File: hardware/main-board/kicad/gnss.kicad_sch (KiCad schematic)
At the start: 39 parts, among them J301 U.FL, J302 UM980_AUX, U301 UM980, U302 TPS22945DCKR

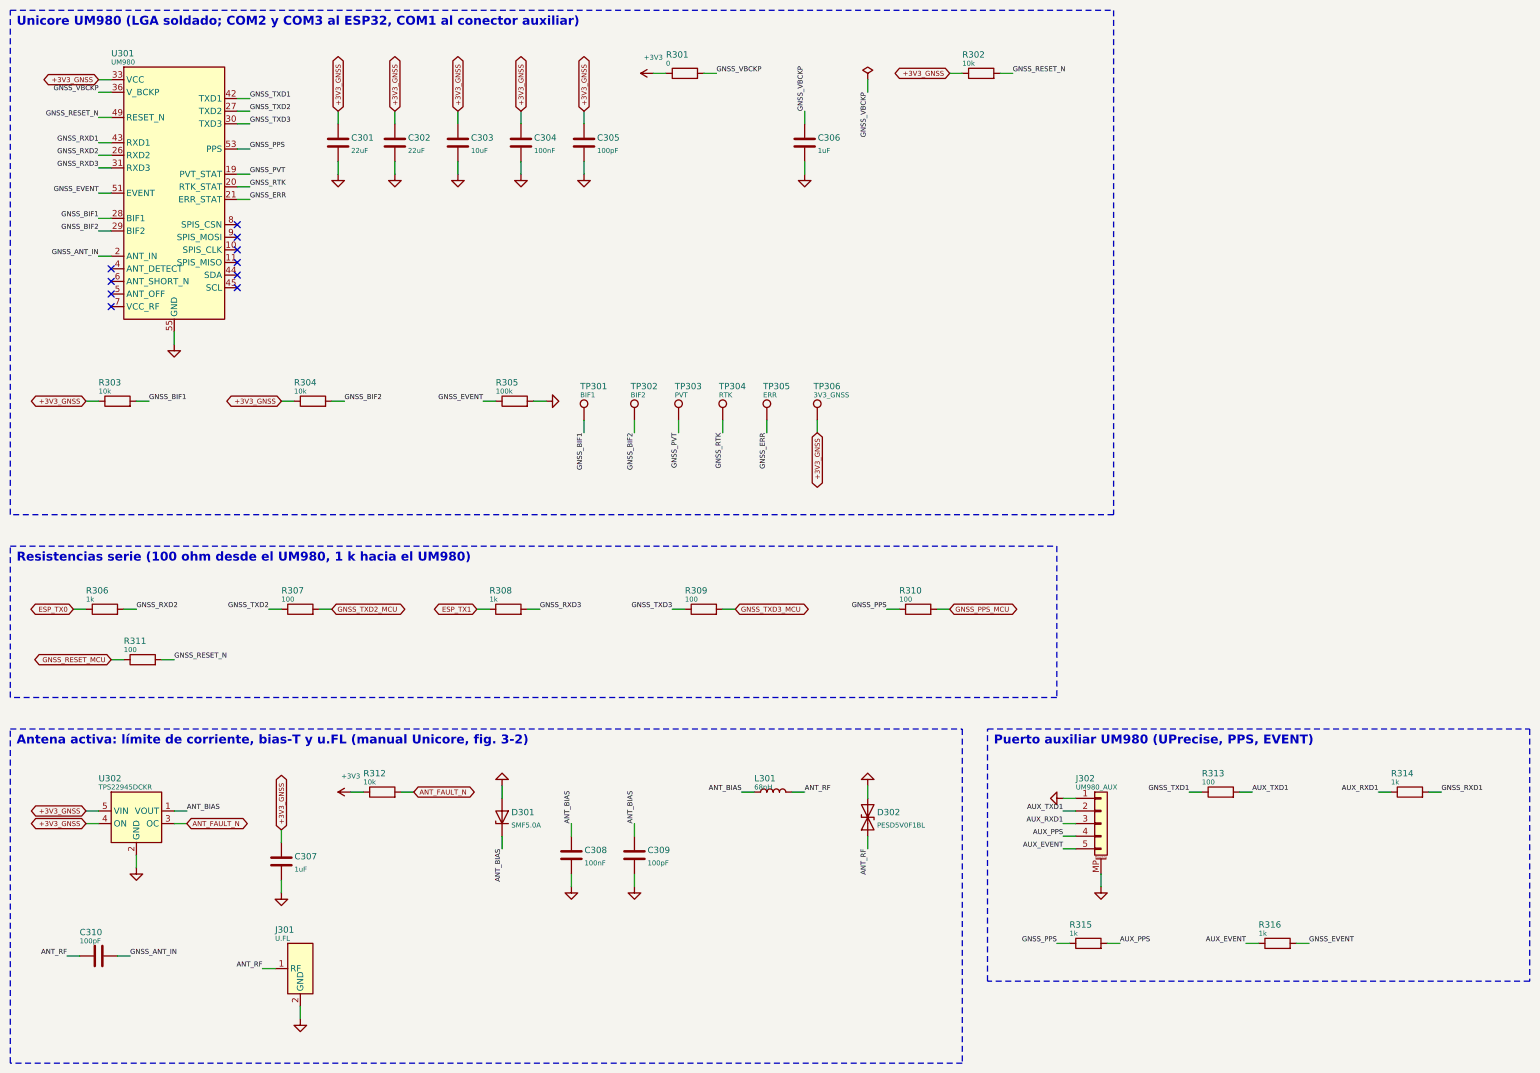
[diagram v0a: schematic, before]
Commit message: Placa principal v0.2: UM980 y BMI088 por cable, conectores hacia cantos o zonas libres, placa panel-usb y un solo panel para JLCPCB
- 46 x 64 mm, 4 capas. El UM980 queda en su carrier BDLX por J301 (GH 8) con 5 V conmutable
  (TPS63070, GPIO45) y el BMI088 vuelve a la tapa por I2C en un segundo bus (J405, GH 7).
- Todos los conectores de cable son GH o SH de 8 pines o menos (kit del propietario), salvo la
  batería (PH 2). Cada uno apunta a un canto o a una zona libre con sitio para la clavija
  enchufada y su cable: áreas de regla clavija_* en el DRC y kicad/plugs.json para el CAD.
- La placa sube 2.5 mm en el tubo (z 23.5-87.5) para que las clavijas del canto inferior tengan
  7.6 mm hasta la base; rieles propuestos en z 39-90 y agujeros nuevos. Comprobada en FreeCAD
  contra V2.2 con modelos 3D y clavijas: sin choques.
- Cargador según el ejemplo de TI: bootstrap junto a sus pines (0.9 y 1.6 mm), salida en abanico
  de la fila inferior y potencia solo por capas externas.
- Placa panel-usb (USB-C a ras de la tapa del panel, GH 8 a J101) y panel de las dos placas con un
  BOM y un CPL (panelize.py, 82.8 x 78 mm).
- Serigrafía sin solapes (silk_clean.py) y logotipo de TresVizo con www.tresvizo.com.
- ERC 0; DRC con 0 errores, 0 avisos, 0 sin conectar y 0 diferencias de paridad en las dos
  placas y el panel. Costo estimado de montaje y piezas: 211 USD por 5 juegos en un panel, sin
  el PCB desnudo.
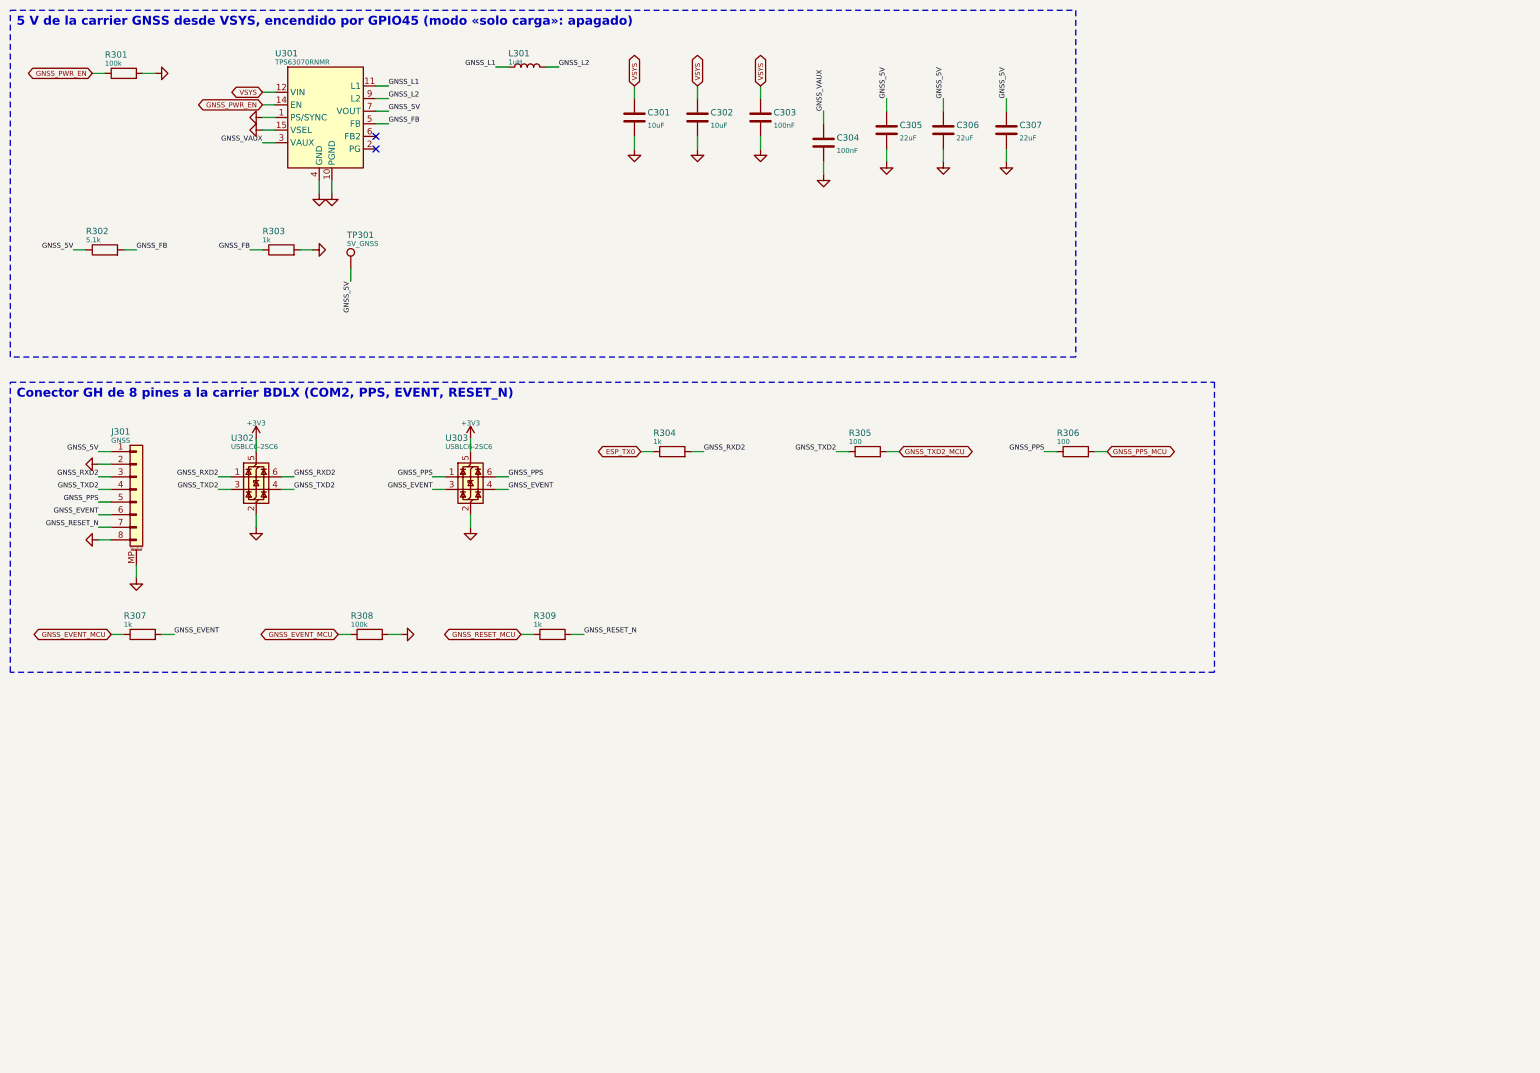
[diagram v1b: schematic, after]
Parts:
- removed C308: 100nF, Capacitor_SMD:C_0402_1005Metric, symbol Device:C
- removed C309, C310: 100pF, Capacitor_SMD:C_0402_1005Metric, symbol Device:C
- removed D301: SMF5.0A, tresvizo_lcsc:SOD-123FL_L2.7-W1.8-LS3.8-RD, symbol Device:D_Zener
- removed D302: PESD5V0F1BL, tresvizo_lcsc:SOD-882_L1.0-W0.6-BI, symbol Device:D_TVS
- removed J302: UM980_AUX, tresvizo_lcsc:CONN-SMD_5P-P1.00_BM05B-SRSS-TB, symbol Connector_Generic_MountingPin:Conn_01x05_MountingPin
- removed R310, R311, R313: 100, Resistor_SMD:R_0402_1005Metric, symbol Device:R
- removed R312: 10k, Resistor_SMD:R_0402_1005Metric, symbol Device:R
- removed R314, R315, R316: 1k, Resistor_SMD:R_0402_1005Metric, symbol Device:R
- removed TP302: BIF2, TestPoint:TestPoint_Pad_D1.0mm, symbol Connector:TestPoint
- removed TP303: PVT, TestPoint:TestPoint_Pad_D1.0mm, symbol Connector:TestPoint
- removed TP304: RTK, TestPoint:TestPoint_Pad_D1.0mm, symbol Connector:TestPoint
- removed TP305: ERR, TestPoint:TestPoint_Pad_D1.0mm, symbol Connector:TestPoint
- removed TP306: 3V3_GNSS, TestPoint:TestPoint_Pad_D1.0mm, symbol Connector:TestPoint
- added U303: USBLC6-2SC6, tresvizo_lcsc:SOT-23-6_L2.9-W1.6-P0.95-LS2.8-BL, symbol Power_Protection:USBLC6-2SC6
- C301, C302: value 22uF -> 10uF; LCSC C45783 -> C15850; MPN CL21A226MAQNNNE -> CL21A106KAYNNNE
- C303: value 10uF -> 100nF; footprint Capacitor_SMD:C_0805_2012Metric -> Capacitor_SMD:C_0402_1005Metric; LCSC C15850 -> C307331; MPN CL21A106KAYNNNE -> CL05B104KB54PNC
- C305: value 100pF -> 22uF; footprint Capacitor_SMD:C_0402_1005Metric -> Capacitor_SMD:C_0805_2012Metric; LCSC C1546 -> C45783; MPN 0402CG101J500NT -> CL21A226MAQNNNE
- C306, C307: value 1uF -> 22uF; footprint Capacitor_SMD:C_0402_1005Metric -> Capacitor_SMD:C_0805_2012Metric; LCSC C52923 -> C45783; MPN CL05A105KA5NQNC -> CL21A226MAQNNNE
- J301: value U.FL -> GNSS; footprint tresvizo_lcsc:IPEX-SMD_BWIPX-1-001E -> tresvizo_lcsc:CONN-SMD_8P-P1.25_XUNPU-WAFER-GH1.25-8PWB; symbol tresvizo:U.FL -> Connector_Generic_MountingPin:Conn_01x08_MountingPin; LCSC C5137195 -> C3029383; MPN BWU.FL-IPEX1 -> WAFER-GH1.25-8PWB
- L301: value 68nH -> 1uH; footprint tresvizo_lcsc:L0603 -> tresvizo_lcsc:L2520; LCSC C86135 -> C435392; MPN LQW18AN68NG00D -> DFE252012F-1R0M=P2
- R301: value 0 -> 100k; LCSC C17168 -> C25741; MPN 0402WGF0000TCE -> 0402WGF1003TCE
- R302: value 10k -> 5.1k; LCSC C25744 -> C25905; MPN 0402WGF1002TCE -> 0402WGF5101TCE
- R303, R304: value 10k -> 1k; LCSC C25744 -> C11702; MPN 0402WGF1002TCE -> 0402WGF1001TCE
- R305: value 100k -> 100; LCSC C25741 -> C25076; MPN 0402WGF1003TCE -> 0402WGF1000TCE
- R306: value 1k -> 100; LCSC C11702 -> C25076; MPN 0402WGF1001TCE -> 0402WGF1000TCE
- R307, R309: value 100 -> 1k; LCSC C25076 -> C11702; MPN 0402WGF1000TCE -> 0402WGF1001TCE
- R308: value 1k -> 100k; LCSC C11702 -> C25741; MPN 0402WGF1001TCE -> 0402WGF1003TCE
- TP301: value BIF1 -> 5V_GNSS
- U301: value UM980 -> TPS63070RNMR; footprint tresvizo:UM980 -> tresvizo_lcsc:VQFN-15_L3.0-W2.5-P0.50-BL; symbol tresvizo:UM980 -> tresvizo:TPS63070; LCSC (none) -> C109322; MPN UM980 -> TPS63070RNMR
- U302: value TPS22945DCKR -> USBLC6-2SC6; footprint tresvizo_lcsc:SC-70-5_L2.1-W1.3-P0.65-LS2.1-BL -> tresvizo_lcsc:SOT-23-6_L2.9-W1.6-P0.95-LS2.8-BL; symbol tresvizo:TPS22945 -> Power_Protection:USBLC6-2SC6; LCSC C47507 -> C2687116; MPN TPS22945DCKR -> USBLC6-2SC6
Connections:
- net ANT_FAULT_N is gone; now on net GNSS_TXD2: U302.3 (I/O2)
- net GNSS_TXD3_MCU is gone; now on net GNSS_RESET_N: R309.2
- net +3V3: now also U302.5 (VBUS), U303.5 (VBUS); no longer R301.1
- net ESP_TX0: now also R304.1; no longer R306.1
- net GND: now also J301.8 (Pin_8), J301.MP (MountPin), R301.2, R303.2, R308.2, U301.10 (PGND), U301.15 (VSEL), U301.4 (GND), U303.2 (GND); no longer J301.3 (GND), R305.2, U301.12 (GND), U301.14 (GND), U301.3 (GND), U301.32 (GND), U301.37 (GND), U301.41 (GND), U301.48 (GND), U301.55 (GND)
- net GNSS_EVENT: now also J301.6 (Pin_6), R307.2, U303.3 (I/O2), U303.4 (I/O2); no longer R305.1, U301.51 (EVENT)
- net GNSS_PPS: now also J301.5 (Pin_5), R306.1, U303.1 (I/O1), U303.6 (I/O1); no longer U301.53 (PPS)
- net GNSS_PPS_MCU: now also R306.2
- net GNSS_RESET_MCU: now also R309.1
- net GNSS_RESET_N: now also J301.7 (Pin_7); no longer R302.2, U301.49 (RESET_N)
- net GNSS_RXD2: now also J301.3 (Pin_3), R304.2, U302.1 (I/O1), U302.6 (I/O1); no longer R306.2, U301.26 (RXD2)
- net GNSS_TXD2: now also J301.4 (Pin_4), R305.1, U302.4 (I/O2); no longer R307.1, U301.27 (TXD2)
- net GNSS_TXD2_MCU: now also R305.2; no longer R307.2
- net GNSS_L1: now reaches U301.11 (L1)
- net GNSS_L1: now also L301.1
- net GNSS_FB: now reaches U301.5 (FB)
- net GNSS_FB: now also R302.2, R303.1
- net GNSS_5V: now reaches U301.7 (VOUT)
- net GNSS_5V: now also C305.1, C306.1, C307.1, J301.1 (Pin_1), R302.1, TP301.1
- net GNSS_L2: now reaches U301.9 (L2)
- net GNSS_L2: now also L301.2
- removed net +3V3_GNSS: C301.1, C302.1, C303.1, C304.1, C305.1, C307.1, R302.1, R303.1, R304.1, U301.33 (VCC), U301.34 (VCC), U302.4 (ON), U302.5 (VIN)
- removed net ANT_BIAS: L301.1, U302.1 (VOUT)
- removed net ANT_RF: J301.1 (RF), L301.2
- net ESP_TX1 renamed GNSS_EVENT_MCU
- net GNSS_EVENT_MCU: now also R307.1
- net GNSS_ANT_IN: no longer names the net of U301.2 (PG)
- removed net GNSS_BIF1: R303.2, TP301.1, U301.28 (BIF1)
- removed net GNSS_BIF2: R304.2, U301.29 (BIF2)
- removed net GNSS_ERR: U301.21 (ERR_STAT)
- removed net GNSS_PVT: U301.19 (PVT_STAT)
- removed net GNSS_RTK: U301.20 (RTK_STAT)
- removed net GNSS_RXD1: U301.43 (RXD1)
- removed net GNSS_RXD3: R308.2, U301.31 (RXD3)
- removed net GNSS_TXD1: U301.42 (TXD1)
- removed net GNSS_TXD3: R309.1, U301.30 (TXD3)
- removed net GNSS_VBCKP: C306.1, R301.2, U301.36 (V_BCKP)
- new net GNSS_PWR_EN: R301.1, U301.14 (EN)
- new net GNSS_VAUX: C304.1, U301.3 (VAUX)
- new net VSYS: C301.1, C302.1, C303.1, U301.12 (VIN)
- no-connect marks 10 -> 2
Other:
- note added: "5 V de la carrier GNSS desde VSYS, encendido por GPIO45 (modo «solo carga»: apagado)"
- note added: "Conector GH de 8 pines a la carrier BDLX (COM2, PPS, EVENT, RESET_N)"
- note removed: "Antena activa: límite de corriente, bias-T y u.FL (manual Unicore, fig. 3-2)"
- note removed: "Puerto auxiliar UM980 (UPrecise, PPS, EVENT)"
- note removed: "Resistencias serie (100 ohm desde el UM980, 1 k hacia el UM980)"
- note removed: "Unicore UM980 (LGA soldado; COM2 y COM3 al ESP32, COM1 al conector auxiliar)"
- title: GNSS UM980 y antena -> GNSS: carrier UM980 por conector y su 5 V
- moved on the sheet: C301, C302, C303, C304, C305, C306, C307, L301, R301, R302, R303, R304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

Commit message: Placa principal v0.2: ESP32-S3-WROOM-1-N16R2 en lugar del MINI-1 y sin LEDs del panel
- U201 = ESP32-S3-WROOM-1-N16R2 (C2913205): 16 MB de flash y 2 MB de PSRAM quad. Huella y
  modelos de LCSC; el .step se corrió 3.65 mm para que coincida con su .wrl y la huella.
- GPIO nuevos para rutear el módulo en la misma placa: microSD CLK 6, CMD 7, D0 5, D1 4, D2 16,
  D3 15 y detección 17; UART del GNSS TX 8 / RX 9; PPS 10, EVENT 11, RESET 12; I2C 13/14;
  IMU 41/42 con INT1 2 e INT3 1; botón 18; puntos de prueba en 35, 36 y 37. README y pinout
  con el mapa para el firmware.
- Fuera J406, sus resistencias y la del STAT del cargador: la carcasa V2.3 no lleva LEDs.
- Misma placa de 46 x 64 mm. H1 pasa a (12.0, 9.6) y el corte del riel +X frente a la antena a
  v 15.1-34.0; antena sin cobre en u 0-6.7, v 15.7-33.7.
- R108 sale de debajo de los pines de la microSD (el ruteador se ciclaba entre SD_D3 y
  CHG_INT_N) y el divisor de TS va bajo L102.
- BUCK_SW y el PGND de U105 prerruteados: la vía que el ruteador ponía junto a L102 hacía caer
  el relleno de zonas de KiCad 10 (-11, también en kicad-cli). route_rest guarda las pistas que
  arranca mientras dura el ruteo.
- DRC 0, sin conexiones pendientes y con paridad en la placa y en el panel; ERC 0. Costo
  estimado 206.86 USD por 5 juegos (montaje + piezas, sin PCB).
- Carcasa V2.3: H1 en z 77.9, riel +X cortado en z 53.7-72.4, placa superior recortada frente
  a la antena y SMA de la carrier con las medidas de la foto. Placa nueva contra la carcasa:
  0 mm3 de choques.
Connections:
- net ESP_TX0 renamed GNSS_TX_MCU
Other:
- moved on the sheet: R304, R305, R306
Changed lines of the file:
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@@
 		(company "TresVizo")
 		(comment 1 "Exploratorio: no fabricado ni probado")
-		(comment 2 "ESP32-S3-MINI-1-N4R2 + BQ25798 (1S; 2S por variante); GNSS e IMU por conector")
+		(comment 2 "ESP32-S3-WROOM-1-N16R2 + BQ25798 (1S; 2S por variante); GNSS e IMU por conector")
 		(comment 3 "JLCPCB 4 capas JLC04161H-7628")
 	)
@@
 	(symbol
 		(lib_id "Device:R")
-		(at 146.05 106.68 90)
+		(at 149.86 106.68 90)
 		(unit 1)
 		(exclude_from_sim no)
@@
 		(dnp no)
 		(property "Reference" "R304"
-			(at 142.24 103.664 270)
+			(at 146.05 103.664 270)
 			(effects
 				(font
@@
 		)
 		(property "Value" "1k"
-			(at 142.24 105.264 270)
+			(at 146.05 105.264 270)
 			(effects
 				(font
@@
 		)
 		(property "Footprint" "Resistor_SMD:R_0402_1005Metric"
-			(at 146.05 106.68 0)
+			(at 149.86 106.68 0)
 			(effects
 				(font
@@
 		)
 		(property "Datasheet" ""
-			(at 146.05 106.68 0)
+			(at 149.86 106.68 0)
 			(effects
 				(font
@@
 			)
 		)
-		(property "Description" "GPIO43 (U0TXD) -> RXD2 de la carrier"
-			(at 146.05 106.68 0)
+		(property "Description" "GPIO8 (TX de la UART del GNSS) -> RXD2 de la carrier"
+			(at 149.86 106.68 0)
 			(effects
 				(font
@@
 		)
 		(property "MPN" "0402WGF1001TCE"
-			(at 146.05 106.68 0)
+			(at 149.86 106.68 0)
 			(effects
 				(font
@@
 		)
 		(property "LCSC" "C11702"
-			(at 146.05 106.68 0)
+			(at 149.86 106.68 0)
 			(effects
 				(font
@@
 	)
 	(wire
-		(pts (xy 142.24 106.68) (xy 139.7 106.68))
+		(pts (xy 146.05 106.68) (xy 143.51 106.68))
 		(stroke
 			(width 0)
@@
 		)
 	)
-	(global_label "ESP_TX0"
+	(global_label "GNSS_TX_MCU"
 		(shape bidirectional)
-		(at 139.7 106.68 180)
+		(at 143.51 106.68 180)
 		(fields_autoplaced yes)
 		(effects
@@
 		)
 		(property "Intersheetrefs" "${INTERSHEET_REFS}"
-			(at 139.7 106.68 0)
+			(at 143.51 106.68 0)
 			(effects
 				(font
@@
 	)
 	(wire
-		(pts (xy 149.86 106.68) (xy 152.4 106.68))
+		(pts (xy 153.67 106.68) (xy 156.21 106.68))
 		(stroke
 			(width 0)
@@
 	)
 	(label "GNSS_RXD2"
-		(at 152.4 106.68 0)
+		(at 156.21 106.68 0)
 		(fields_autoplaced yes)
 		(effects
@@
 	(symbol
 		(lib_id "Device:R")
-		(at 185.42 106.68 90)
+		(at 189.23 106.68 90)
 		(unit 1)
 		(exclude_from_sim no)
@@
 		(dnp no)
 		(property "Reference" "R305"
-			(at 181.61 103.664 270)
+			(at 185.42 103.664 270)
 			(effects
 				(font
@@
 		)
 		(property "Value" "100"
-			(at 181.61 105.264 270)
+			(at 185.42 105.264 270)
 			(effects
 				(font
@@
 		)
 		(property "Footprint" "Resistor_SMD:R_0402_1005Metric"
-			(at 185.42 106.68 0)
+			(at 189.23 106.68 0)
 			(effects
 				(font
@@
 		)
 		(property "Datasheet" ""
-			(at 185.42 106.68 0)
+			(at 189.23 106.68 0)
 			(effects
 				(font
@@
 			)
 		)
-		(property "Description" "TXD2 de la carrier -> GPIO44 (U0RXD)"
-			(at 185.42 106.68 0)
+		(property "Description" "TXD2 de la carrier -> GPIO9 (RX de la UART del GNSS)"
+			(at 189.23 106.68 0)
 			(effects
 				(font
@@
 		)
 		(property "MPN" "0402WGF1000TCE"
-			(at 185.42 106.68 0)
+			(at 189.23 106.68 0)
 			(effects
 				(font
@@
 		)
 		(property "LCSC" "C25076"
-			(at 185.42 106.68 0)
+			(at 189.23 106.68 0)
 			(effects
 				(font
@@
 	)
 	(wire
-		(pts (xy 181.61 106.68) (xy 179.07 106.68))
+		(pts (xy 185.42 106.68) (xy 182.88 106.68))
 		(stroke
 			(width 0)
@@
 	)
 	(label "GNSS_TXD2"
-		(at 179.07 106.68 180)
+		(at 182.88 106.68 180)
 		(fields_autoplaced yes)
 		(effects
@@
 	)
 	(wire
-		(pts (xy 189.23 106.68) (xy 191.77 106.68))
+		(pts (xy 193.04 106.68) (xy 195.58 106.68))
 		(stroke
 			(width 0)
@@
 	(global_label "GNSS_TXD2_MCU"
 		(shape bidirectional)
-		(at 191.77 106.68 0)
+		(at 195.58 106.68 0)
 		(fields_autoplaced yes)
 		(effects
@@
 		)
 		(property "Intersheetrefs" "${INTERSHEET_REFS}"
-			(at 191.77 106.68 0)
+			(at 195.58 106.68 0)
 			(effects
 				(font
@@
 	(symbol
 		(lib_id "Device:R")
-		(at 227.33 106.68 90)
+		(at 232.41 106.68 90)
 		(unit 1)
 		(exclude_from_sim no)
@@
 		(dnp no)
 		(property "Reference" "R306"
-			(at 223.52 103.664 270)
+			(at 228.6 103.664 270)
 			(effects
 				(font
@@
 		)
 		(property "Value" "100"
-			(at 223.52 105.264 270)
+			(at 228.6 105.264 270)
 			(effects
 				(font
@@
 		)
 		(property "Footprint" "Resistor_SMD:R_0402_1005Metric"
-			(at 227.33 106.68 0)
+			(at 232.41 106.68 0)
 			(effects
 				(font
@@
 		)
 		(property "Datasheet" ""
-			(at 227.33 106.68 0)
+			(at 232.41 106.68 0)
 			(effects
 				(font
@@
 			)
 		)
-		(property "Description" "PPS -> GPIO1"
-			(at 227.33 106.68 0)
+		(property "Description" "PPS -> GPIO10"
+			(at 232.41 106.68 0)
 			(effects
 				(font
@@
 		)
 		(property "MPN" "0402WGF1000TCE"
-			(at 227.33 106.68 0)
+			(at 232.41 106.68 0)
 			(effects
 				(font
@@
 		)
 		(property "LCSC" "C25076"
-			(at 227.33 106.68 0)
+			(at 232.41 106.68 0)
 			(effects
 				(font
@@
 	)
 	(wire
-		(pts (xy 223.52 106.68) (xy 220.98 106.68))
+		(pts (xy 228.6 106.68) (xy 226.06 106.68))
 		(stroke
 			(width 0)
@@
 	)
 	(label "GNSS_PPS"
-		(at 220.98 106.68 180)
+		(at 226.06 106.68 180)
 		(fields_autoplaced yes)
 		(effects
@@
 	)
 	(wire
-		(pts (xy 231.14 106.68) (xy 233.68 106.68))
+		(pts (xy 236.22 106.68) (xy 238.76 106.68))
 		(stroke
 			(width 0)
@@
 	(global_label "GNSS_PPS_MCU"
 		(shape bidirectional)
-		(at 233.68 106.68 0)
+		(at 238.76 106.68 0)
 		(fields_autoplaced yes)
 		(effects
@@
 		)
 		(property "Intersheetrefs" "${INTERSHEET_REFS}"
-			(at 233.68 106.68 0)
+			(at 238.76 106.68 0)
 			(effects
 				(font
@@
 			)
 		)
-		(property "Description" "GPIO5 -> EVENT"
+		(property "Description" "GPIO11 -> EVENT"
 			(at 39.37 143.51 0)
 			(effects
@@
 			)
 		)
-		(property "Description" "GPIO4 en drenador abierto; la BDLX no saca RESET_N"
+		(property "Description" "GPIO12 en drenador abierto; la BDLX no saca RESET_N"
 			(at 121.92 143.51 0)
 			(effects
@@
 	(rectangle
 		(start 12.7 92.71)
-		(end 255.27 151.13)
+		(end 259.08 151.13)
 		(stroke
 			(width 0.1524)
